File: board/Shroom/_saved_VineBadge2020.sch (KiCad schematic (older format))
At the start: 66 parts, among them IC1 ATTINY20-X, J1 CONN-TAGCONNECT-TC2050, SW1 SW_SPDT, SW2 SW_Push

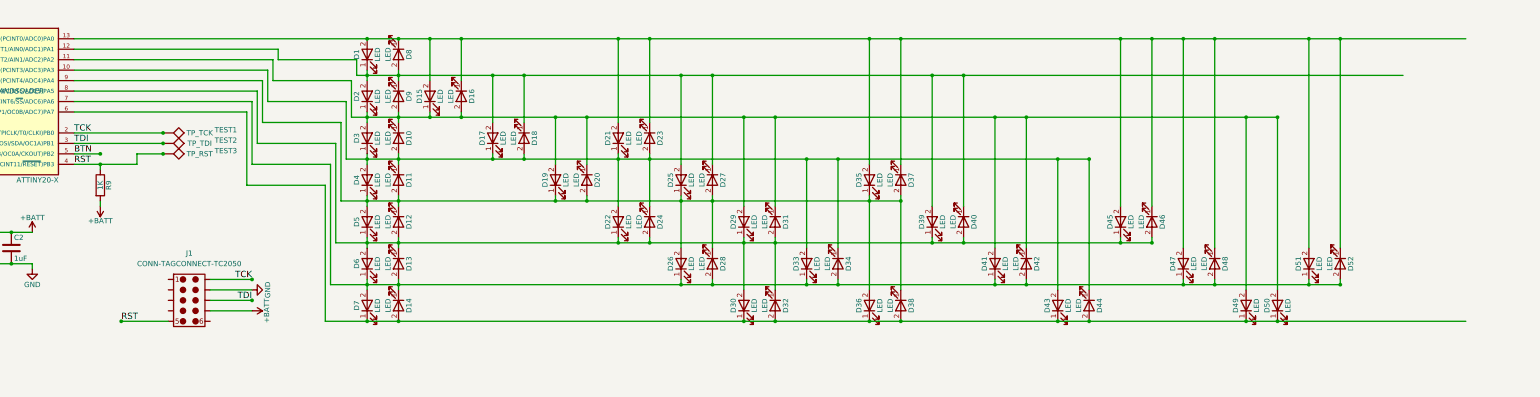
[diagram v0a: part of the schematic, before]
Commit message: added a list of LED settings
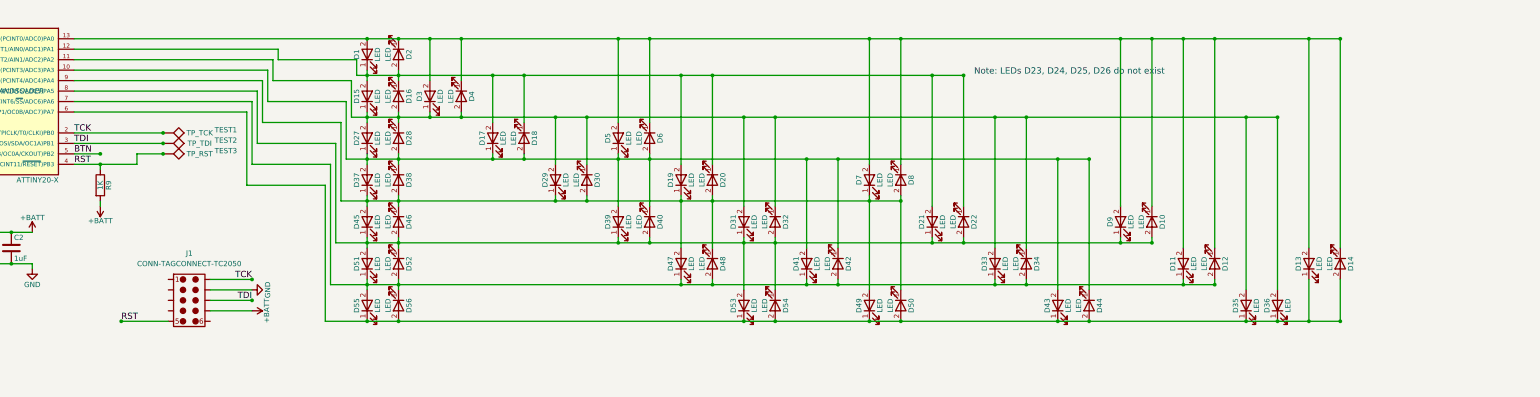
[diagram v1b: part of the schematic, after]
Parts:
- renumbered D46 to D10, D47 to D11, D48 to D12, D51 to D13, D52 to D14, D2 to D15, D9 to D16, D25 to D19, D8 to D2, D27 to D20, D39 to D21, D40 to D22, D3 to D27, D10 to D28, D19 to D29, D15 to D3, D20 to D30, D29 to D31, D31 to D32, D41 to D33, D42 to D34, D49 to D35, D50 to D36, D4 to D37, D11 to D38, D22 to D39, D16 to D4, D24 to D40, D33 to D41, D34 to D42, D5 to D45, D12 to D46, D26 to D47, D28 to D48, D36 to D49, D21 to D5, D38 to D50, D6 to D51, D13 to D52, D30 to D53, D32 to D54, D7 to D55, D14 to D56, D23 to D6, D35 to D7, D37 to D8, D45 to D9
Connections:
- net at D35.1 (K), D36.1 (K), D43.1 (K)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: now also D13.1 (K), D14.2 (A)
- net at D11.1 (K), D12.2 (A), D33.1 (K)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: no longer D13.1 (K), D14.2 (A)
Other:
- note added: "Note: LEDs D23, D24, D25, D26 do not exist"
